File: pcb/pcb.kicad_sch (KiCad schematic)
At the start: 104 parts, among them J1 44P PATA, J2 CEZIF, J3 S6, U1 JM20330, U2 SM2258XT, U3 FlashBGA152, U5 SY8008, U6 SY8008, U7 TX4314, U8 SY8008, Y1 25MHz, Y2 50MHz

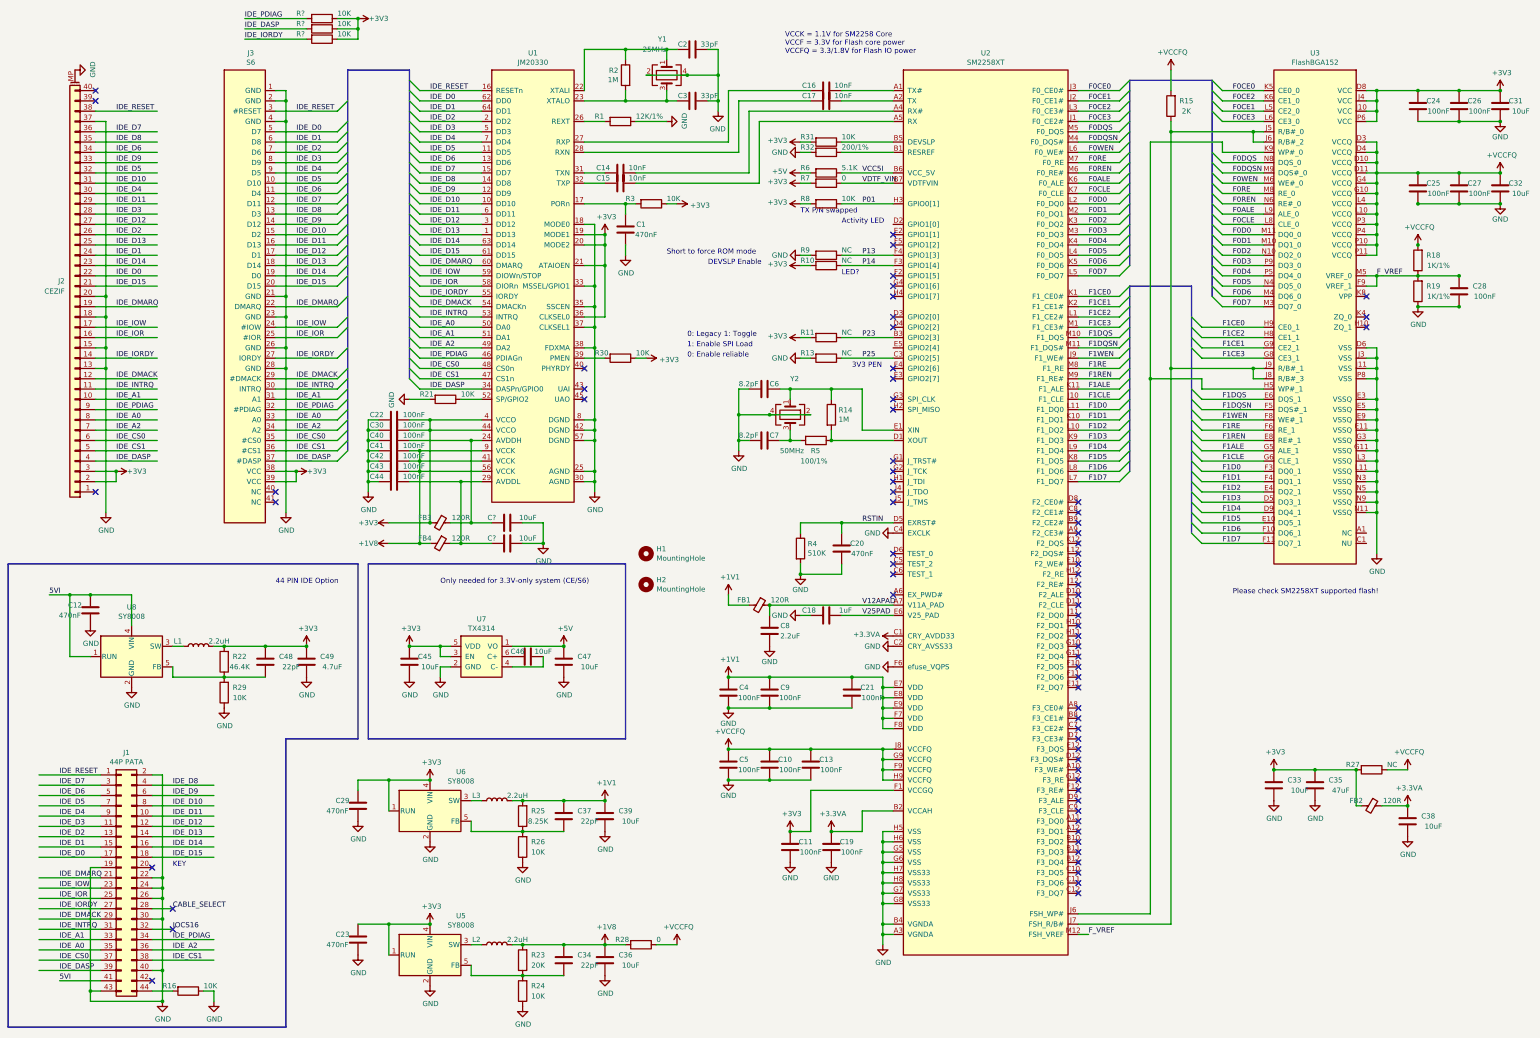
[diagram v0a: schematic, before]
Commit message: Upgrade to new nightly, remove 5V charge pump, add UDMA speed option resistor
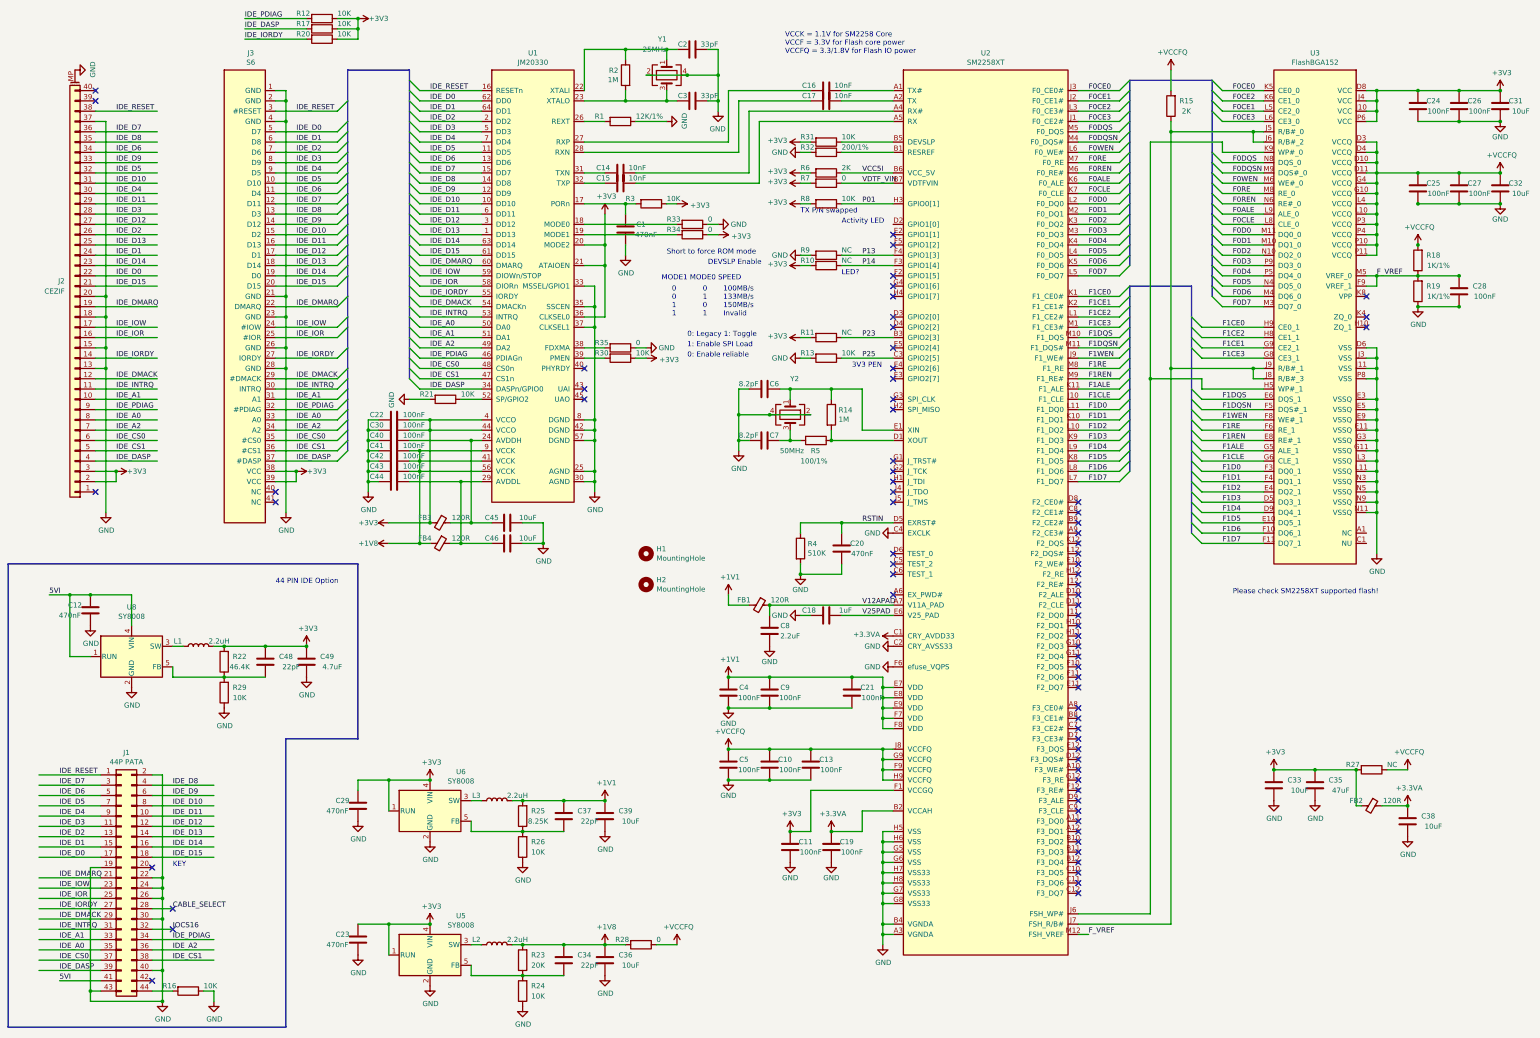
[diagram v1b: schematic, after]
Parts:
- removed C45, C46, C47: 10uF, Capacitor_SMD:C_0402_1005Metric, symbol Device:C
- removed U7: TX4314, Package_TO_SOT_SMD:SOT-23-6, symbol symbols:TX4314
- added R33, R34, R35: 0, Resistor_SMD:R_0402_1005Metric, symbol Device:R
- R13: value NC -> 10K
- R6: value 5.1K -> 2K
- gave numbers to parts that had none: 5
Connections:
- net +5V is gone; now on net +3V3: R6.2
- net +3V3: now also R34.1; no longer U1.19 (MODE1)
- net GND: now also R33.1, R35.1; no longer U1.18 (MODE0), U1.38 (FDXMA)
- new net: R33.2, U1.18 (MODE0)
- new net: R34.2, U1.19 (MODE1)
- new net: R35.2, U1.38 (FDXMA)
- no-connect marks 73 -> 74
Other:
- note added: "0 0 1 1"
- note added: "0 1 0 1"
- note added: "100MB/s 133MB/s 150MB/s Invalid"
- note added: "MODE1 MODE0 SPEED"
- note removed: "Only needed for 3.3V-only system (CE/S6)"

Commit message: Rev 0.3
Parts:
- removed H1, H2: MountingHole, MountingHole:MountingHole_2.2mm_M2_Pad_Via, symbol Mechanical:MountingHole
- removed R35: 0, Resistor_SMD:R_0402_1005Metric, symbol Device:R
- added H1, H2: MountingHole_Pad, MountingHole:MountingHole_2.2mm_M2_Pad_Via, symbol Mechanical:MountingHole_Pad
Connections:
- net GND: now also U1.38 (FDXMA), H1.1, H2.1
- net IDE_D0: now also J3.19 (D0); no longer J3.5 (D7)
- net IDE_D1: now also J3.17 (D1); no longer J3.6 (D8)
- net IDE_D10: now also J3.10 (D10); no longer J3.15 (D2)
- net IDE_D11: now also J3.12 (D11); no longer J3.16 (D13)
- net IDE_D12: now also J3.14 (D12); no longer J3.17 (D1)
- net IDE_D13: now also J3.16 (D13); no longer J3.18 (D14)
- net IDE_D14: now also J3.18 (D14); no longer J3.19 (D0)
- net IDE_D2: now also J3.15 (D2); no longer J3.7 (D6)
- net IDE_D3: now also J3.13 (D3); no longer J3.8 (D9)
- net IDE_D4: now also J3.11 (D4); no longer J3.9 (D5)
- net IDE_D5: now also J3.9 (D5); no longer J3.10 (D10)
- net IDE_D6: now also J3.7 (D6); no longer J3.11 (D4)
- net IDE_D7: now also J3.5 (D7); no longer J3.12 (D11)
- net IDE_D8: now also J3.6 (D8); no longer J3.13 (D3)
- net IDE_D9: now also J3.8 (D9); no longer J3.14 (D12)
